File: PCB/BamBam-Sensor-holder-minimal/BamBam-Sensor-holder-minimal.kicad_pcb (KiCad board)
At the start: 2 copper layers, 35 x 15.6 mm, 19 parts, among them P1 CONN_01X06, U1 DRV5013AD, U2 DRV5013AD, U3 DRV5013AD

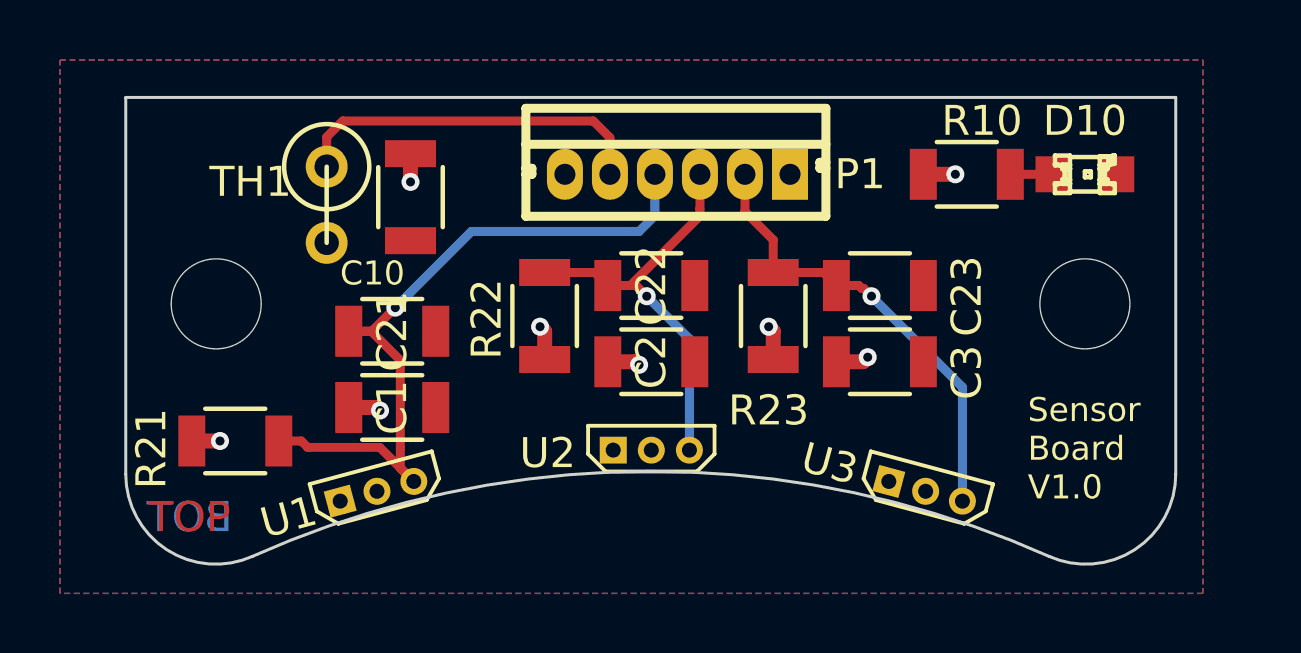
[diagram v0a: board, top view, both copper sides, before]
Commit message: Bohrungen Mount auf 3.2mm vergrößert Bohrungen Hall-Sensoren von 0.5mm auf 0.7mm vergrößert. Versionsnummer angepasst LED-Widerstand angepasst
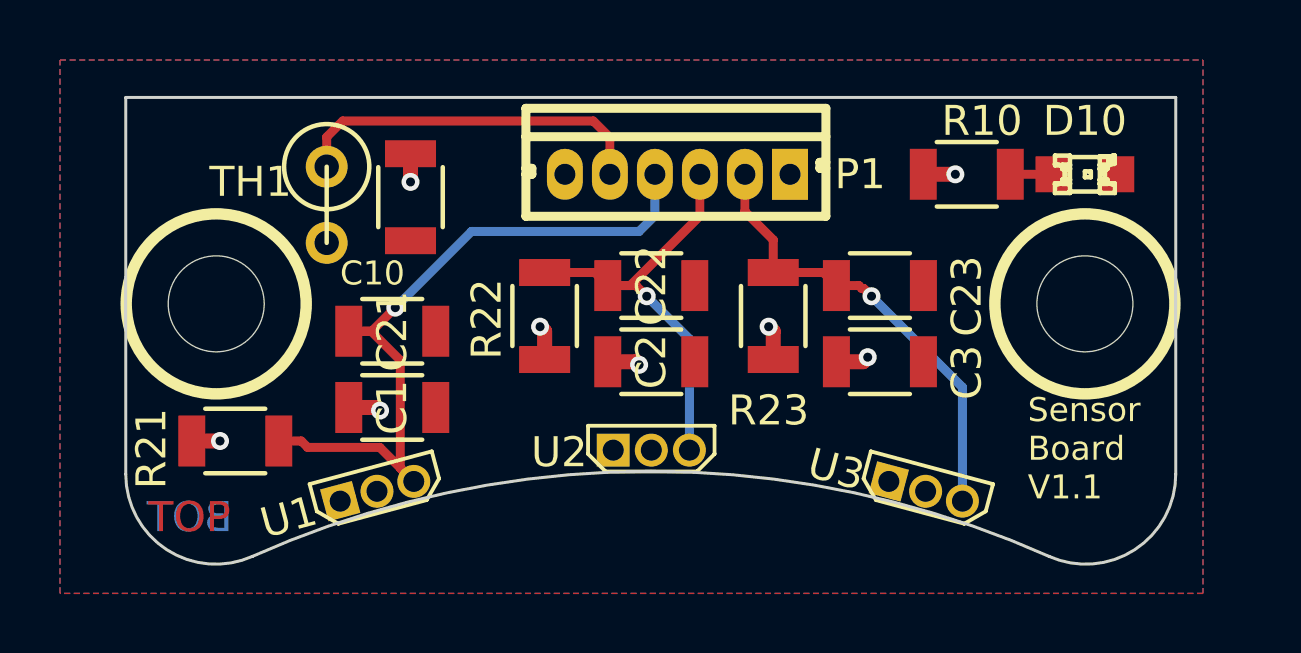
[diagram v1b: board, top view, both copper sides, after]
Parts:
- H1, H2: footprint Mounting_Holes:MountingHole_3mm -> packages:MountingHole_3mm
- R10: value 470 -> 220
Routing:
- net /Temp: track 12.1 -> 13.3 mm
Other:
- board text added: "Sensor Board V1.1"
- board text removed: "Sensor Board V1.0"

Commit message: Anpassung an KiCad > 02/2015 Kleine Korrekturen des Layouts Sensoren um 0.6° weiter auseinander gestellt.
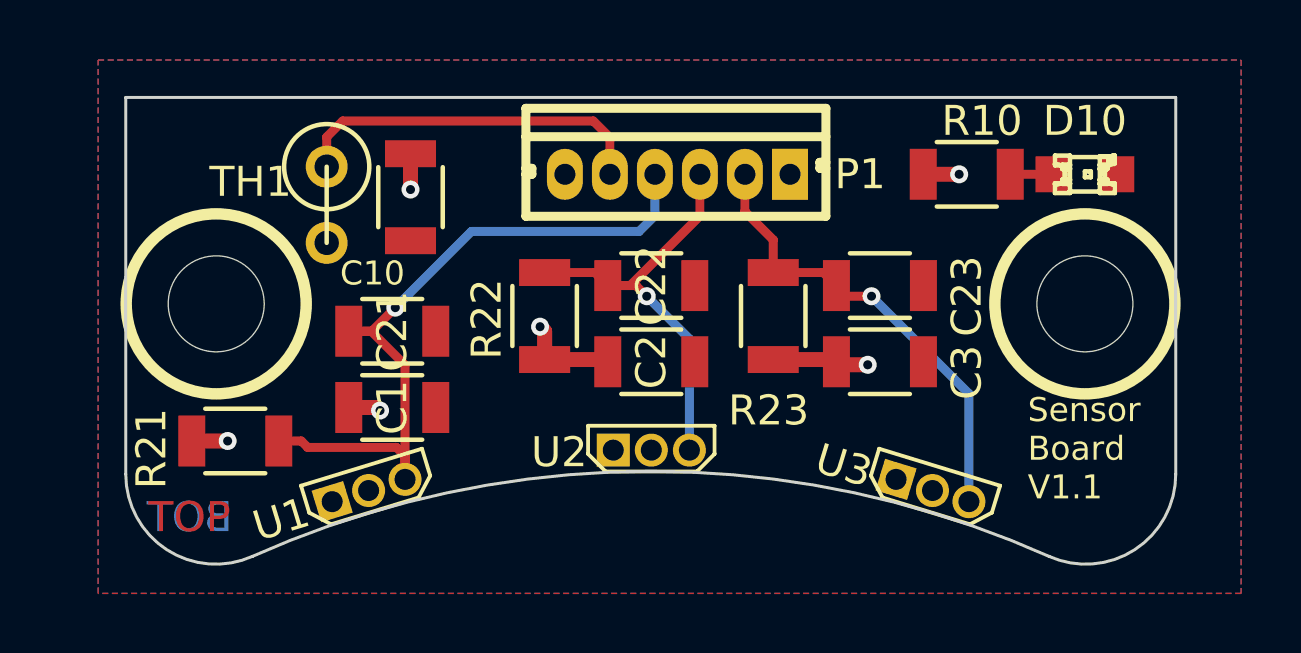
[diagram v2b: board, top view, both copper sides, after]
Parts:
- moved U1 0.28 mm to (143.6, 123.6), turned to 107 degrees
- moved U3 0.23 mm to (162.4, 123.6), turned to 73 degrees
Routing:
- net /Vcc: track 8.55 -> 11.2 mm, vias 8 -> 6
- net /A: track 24.6 -> 25.2 mm

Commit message: Sensoren Pads vergrößert Winkel der Sensorenanordnung überprüft und angepasst.
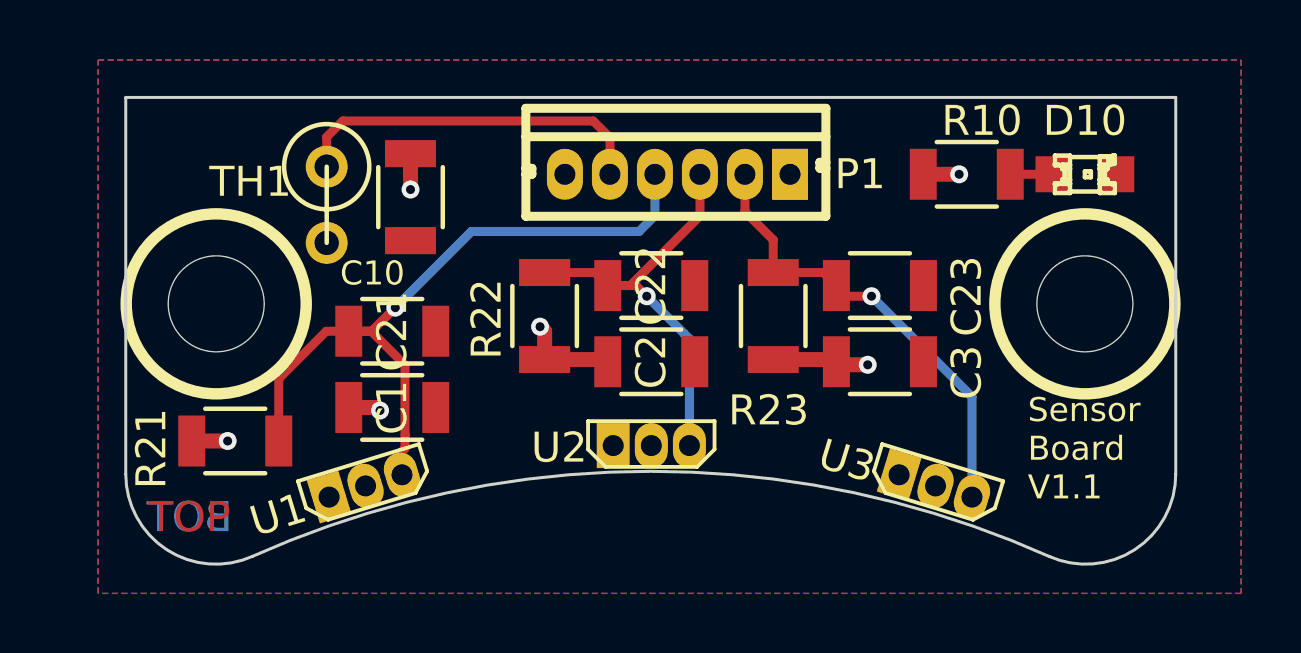
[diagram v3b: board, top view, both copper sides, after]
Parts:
- moved U3 0.18 mm to (162.5, 123.4)
- moved U1 0.18 mm to (143.5, 123.4)
- moved U2 0.15 mm to (153.1, 122.1)
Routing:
- net /A: track 25.2 -> 24.3 mm

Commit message: Die Sensoren sind von der Leiterplattenkante 0.254mm entfernt. Der Anschlussstecker wurde am Mittelsensor ausgerichtet. Die Versionsnummer wurde auf 1.3 angehoben. Layout optimiert, bessere GND-Versorgung.
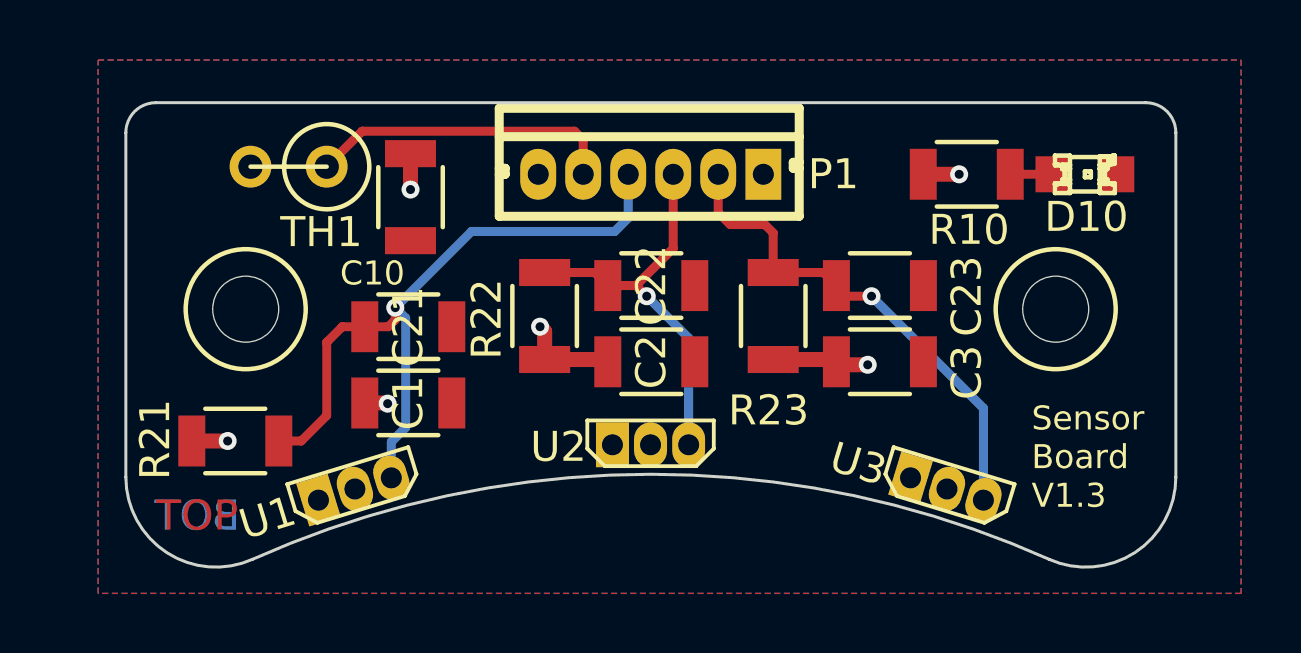
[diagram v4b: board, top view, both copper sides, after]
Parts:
- H2: footprint packages:MountingHole_3mm -> packages:MountingHole_2mm
- moved TH1 1.80 mm to (141.0, 112.8), turned to 180 degrees
- moved H1 1.00 mm to (139.5, 117.5)
- moved H2 0.99 mm to (166.5, 117.5)
- moved P1 0.89 mm to (153.0, 113.0)
- moved C1 0.56 mm to (145.0, 120.7)
- moved C21 0.56 mm to (145.0, 118.1)
- moved U3 0.39 mm to (162.9, 123.5)
- moved U1 0.37 mm to (143.2, 123.5)
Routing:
- net /Temp: track 13.3 -> 10.3 mm
- net /C: track 15.4 -> 16.7 mm
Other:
- board size 35 x 15.6 mm -> 35 x 15.5 mm
- board text added: "Sensor Board V1.3"
- board text removed: "Sensor Board V1.1"
